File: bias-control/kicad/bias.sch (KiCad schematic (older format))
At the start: 26 parts, among them IC1 LT3571EUD#PBF, IC2 ATSAMD21E18A-AFT, IC3 ADP7118ACPZN3.3, J1 Conn_01x04, J2 CX80B1-24P, U1 MCP4726A0T-E_MAY

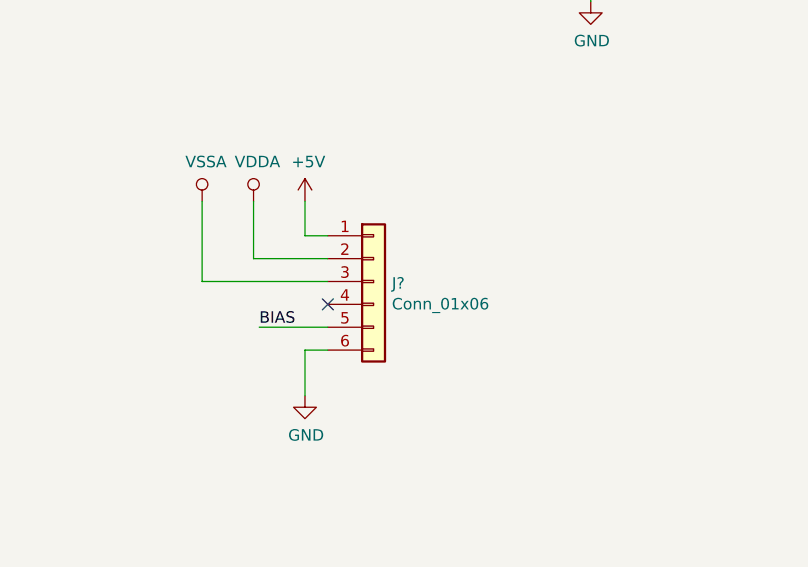
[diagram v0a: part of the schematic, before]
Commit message: change connector to 2x3
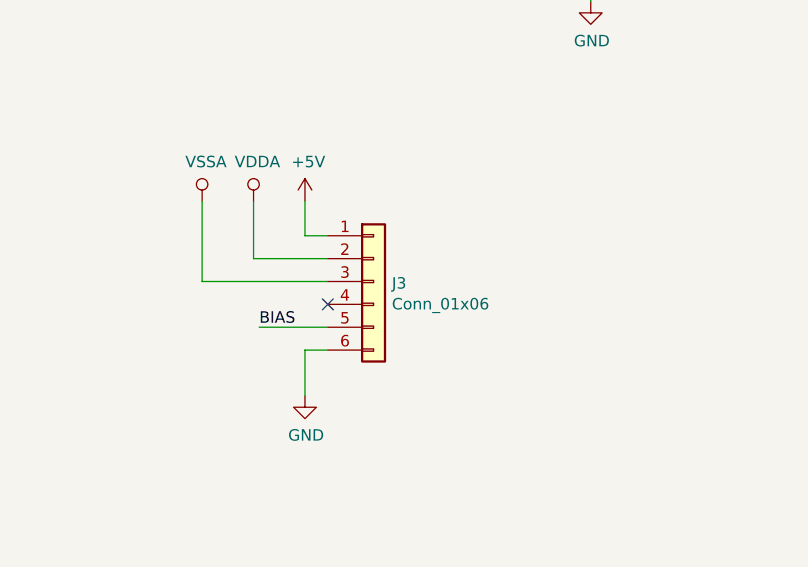
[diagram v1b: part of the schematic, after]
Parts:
- gave numbers to parts that had none: 1
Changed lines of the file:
@@
 	1425 5100 1425 5225
 $Comp
-L Connector_Generic:Conn_01x06 J?
+L Connector_Generic:Conn_01x06 J3
 U 1 1 5DBA004A
 P 9350 5100
-F 0 "J?" H 9430 5092 50  0000 L CNN
+F 0 "J3" H 9430 5092 50  0000 L CNN
 F 1 "Conn_01x06" H 9430 5001 50  0000 L CNN
 F 2 "footprints:PinHeader_2x03_P2.54mm_Vertical" H 9350 5100 50  0001 C CNN
@@
 $EndComp
 $Comp
-L power:VSSA #PWR?
+L power:VSSA #PWR0126
 U 1 1 5DBA2088
 P 8600 4750
-F 0 "#PWR?" H 8600 4600 50  0001 C CNN
+F 0 "#PWR0126" H 8600 4600 50  0001 C CNN
 F 1 "VSSA" H 8617 4923 50  0000 C CNN
 F 2 "" H 8600 4750 50  0001 C CNN
@@
 $EndComp
 $Comp
-L power:VDDA #PWR?
+L power:VDDA #PWR0127
 U 1 1 5DBA264E
 P 8825 4750
-F 0 "#PWR?" H 8825 4600 50  0001 C CNN
+F 0 "#PWR0127" H 8825 4600 50  0001 C CNN
 F 1 "VDDA" H 8842 4923 50  0000 C CNN
 F 2 "" H 8825 4750 50  0001 C CNN

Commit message: tweaks, add octopart BOMs
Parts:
- C2, C4, C7: value 1u -> 2.2u
- IC2: value ATSAMD21E18A-AFT -> ATSAMD21E18A-MUT
- J1: value Conn_01x04 -> ISP
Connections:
- net VDDA: now also J3.3 (Pin_3); no longer J3.2 (Pin_2)
- net VSSA: now also J3.2 (Pin_2); no longer J3.3 (Pin_3)
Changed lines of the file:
@@
 P 3225 4850
 F 0 "C4" H 3317 4896 50  0000 L CNN
-F 1 "1u" H 3317 4805 50  0000 L CNN
+F 1 "2.2u" H 3317 4805 50  0000 L CNN
 F 2 "C_0402_1005Metric" H 3225 4850 50  0001 C CNN
 F 3 "" H 3225 4850 50  0001 C CNN
@@
 P 1425 5000
 F 0 "C2" H 1517 5046 50  0000 L CNN
-F 1 "1u" H 1517 4955 50  0000 L CNN
+F 1 "2.2u" H 1517 4955 50  0000 L CNN
 F 2 "C_0402_1005Metric" H 1425 5000 50  0001 C CNN
 F 3 "" H 1425 5000 50  0001 C CNN
@@
 P 7625 1600
 F 0 "IC2" H 7925 2350 50  0000 L CNN
-F 1 "ATSAMD21E18A-AFT" H 7925 2250 50  0000 L CNN
+F 1 "ATSAMD21E18A-MUT" H 7925 2250 50  0000 L CNN
 F 2 "QFN-32-1EP_5x5mm_Pitch0.5mm" H 8775 2200 50  0001 L CNN
 F 3 "http://www.microchip.com/mymicrochip/filehandler.aspx?ddocname=en590209" H 8775 2100 50  0001 L CNN
@@
 P 10575 3500
 F 0 "J1" H 10655 3492 50  0000 L CNN
-F 1 "Conn_01x04" H 10655 3401 50  0000 L CNN
+F 1 "ISP" H 10655 3401 50  0000 L CNN
 F 2 "POGO_ISP" H 10575 3500 50  0001 C CNN
 F 3 "~" H 10575 3500 50  0001 C CNN
@@
 P 7425 2250
 F 0 "C7" H 7517 2296 50  0000 L CNN
-F 1 "1u" H 7517 2205 50  0000 L CNN
+F 1 "2.2u" H 7517 2205 50  0000 L CNN
 F 2 "C_0402_1005Metric" H 7425 2250 50  0001 C CNN
 F 3 "~" H 7425 2250 50  0001 C CNN
@@
 L power:VSSA #PWR0126
 U 1 1 5DBA2088
+P 8825 4750
+F 0 "#PWR0126" H 8825 4600 50  0001 C CNN
+F 1 "VSSA" H 8842 4923 50  0000 C CNN
+F 2 "" H 8825 4750 50  0001 C CNN
+F 3 "" H 8825 4750 50  0001 C CNN
+	1    8825 4750
+	1    0    0    -1
+$EndComp
+$Comp
+L power:VDDA #PWR0127
+U 1 1 5DBA264E
 P 8600 4750
-F 0 "#PWR0126" H 8600 4600 50  0001 C CNN
-F 1 "VSSA" H 8617 4923 50  0000 C CNN
+F 0 "#PWR0127" H 8600 4600 50  0001 C CNN
+F 1 "VDDA" H 8617 4923 50  0000 C CNN
 F 2 "" H 8600 4750 50  0001 C CNN
 F 3 "" H 8600 4750 50  0001 C CNN
@@
 	1    0    0    -1
 $EndComp
-$Comp
-L power:VDDA #PWR0127
-U 1 1 5DBA264E
-P 8825 4750
-F 0 "#PWR0127" H 8825 4600 50  0001 C CNN
-F 1 "VDDA" H 8842 4923 50  0000 C CNN
-F 2 "" H 8825 4750 50  0001 C CNN
-F 3 "" H 8825 4750 50  0001 C CNN
-	1    8825 4750
-	1    0    0    -1
-$EndComp

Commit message: Fix capacitor value
The datasheet says to use 270nF.
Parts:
- C8: value 10n -> 270n
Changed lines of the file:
@@
 P 6025 5975
 F 0 "C8" H 6117 6021 50  0000 L CNN
-F 1 "10n" H 6117 5930 50  0000 L CNN
+F 1 "270n" H 6117 5930 50  0000 L CNN
 F 2 "C_0402_1005Metric" H 6025 5975 50  0001 C CNN
 F 3 "" H 6025 5975 50  0001 C CNN

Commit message: Switch bias generation board to 4 layers
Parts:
- C8: footprint C_0402_1005Metric -> Capacitor_SMD:C_0805_2012Metric
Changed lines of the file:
@@
 F 0 "C8" H 6117 6021 50  0000 L CNN
 F 1 "270n" H 6117 5930 50  0000 L CNN
-F 2 "C_0402_1005Metric" H 6025 5975 50  0001 C CNN
+F 2 "Capacitor_SMD:C_0805_2012Metric" H 6025 5975 50  0001 C CNN
 F 3 "" H 6025 5975 50  0001 C CNN
 	1    6025 5975

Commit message: Add additional files
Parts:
- removed J2: CX80B1-24P, HRS_CX80B1-24P, symbol CX80B1-24P:CX80B1-24P
- removed U1: MCP4726A0T-E_MAY, footprints:MCP4726A0T-EMAY, symbol MCP4726A0T:MCP4726A0T-E_MAY
- added J2: DF13C-5P-1.25V21, footprints:DF13C-5P-1.25V21, symbol 2020-07-20_16-11-18:DF13C-5P-1.25V21
- added J4: DX07S024WJ3R400, digikey-footprints:USB-C_Female_Vert_DX07S024WJ3R400, symbol dk_USB-DVI-HDMI-Connectors:DX07S024WJ3R400
- added U1: MCP4728, Package_SO:MSOP-10_3x3mm_P0.5mm, symbol Analog_DAC:MCP4728
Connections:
- net labels added: OFFSET
- wire segments 134 -> 153
- no-connect marks 13 -> 2
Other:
- moved on the sheet: C2, J1, R8, R9

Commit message: Tweak layout
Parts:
- R3: value 49.9 -> 10
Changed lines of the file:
@@
 P 5000 6275
 F 0 "R3" V 4925 6275 50  0000 C CNN
-F 1 "49.9" V 5100 6275 50  0000 C CNN
+F 1 "10" V 5100 6275 50  0000 C CNN
 F 2 "R_0402_1005Metric" H 5000 6275 50  0001 C CNN
 F 3 "" H 5000 6275 50  0001 C CNN
